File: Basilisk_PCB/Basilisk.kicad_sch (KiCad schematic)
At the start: 58 parts, among them J1 Conn_01x04, J2 HUB75E, J3 Barrel_Jack, J4 USB_C_Receptacle_USB2.0, Q1 S8050, Q2 S8050, SW1 IO0, SW2 RST, U1 AT25SF081-SSHD-X, U2 ESP32-WROOM-32D, U3 MLX90640, U4 TXS0108EPW, U5 TXS0108EPW, U6 TPS54560BDDA, U7 AMS1117-3.3, U8 FT231XS

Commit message: read thermal camera
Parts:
- added R?: PDV-P8103, OptoDevice:R_LDR_5.0x4.1mm_P3mm_Vertical, symbol Sensor_Optical:A9050
- added R?: 53.6k, Resistor_SMD:R_0805_2012Metric, symbol Device:R
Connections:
- net +3.3V: now also R?.1
- net GND: now also R?.1
- net at U2.6 (IO34): now also R?.2, R?.2
- no-connect marks 24 -> 23
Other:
- note added: "500 - 20kOhm"
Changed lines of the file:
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@@
   (junction (at 88.9 189.23) (diameter 0) (color 0 0 0 0)
+  )
+  (junction (at 240.03 90.17) (diameter 0) (color 0 0 0 0)
   )
   (junction (at 242.57 113.03) (diameter 0) (color 0 0 0 0)
@@
   (no_connect (at 77.47 113.03))
   (no_connect (at 227.33 92.71))
-  (no_connect (at 227.33 90.17))
   (no_connect (at 50.8 173.99))
   (no_connect (at 50.8 171.45))
@@
     (stroke (width 0) (type default) (color 0 0 0 0))
   )
+  (wire (pts (xy 227.33 90.17) (xy 240.03 90.17))
+    (stroke (width 0) (type default) (color 0 0 0 0))
+  )
   (wire (pts (xy 240.03 69.85) (xy 240.03 72.39))
     (stroke (width 0) (type default) (color 0 0 0 0))
@@
     (effects (font (size 1.27 1.27)) (justify left bottom))
   )
+  (text "500 - 20kOhm" (at 246.38 85.09 0)
+    (effects (font (size 1.27 1.27)) (justify left bottom))
+  )
   (text "IO7\nIO8\nIO9\nIO10\nIO6\nIO11" (at 210.82 77.47 0)
     (effects (font (size 1.27 1.27)) (justify left bottom))
@@
   (label "E.5" (at 72.39 100.33 0)
     (effects (font (size 1.27 1.27)) (justify left bottom))
+  )
+  (symbol (lib_id "Sensor_Optical:A9050") (at 240.03 86.36 0) (unit 1)
+    (in_bom yes) (on_board yes) (fields_autoplaced)
+    (property "Reference" "R?" (id 0) (at 242.57 85.0899 0)
+      (effects (font (size 1.27 1.27)) (justify left))
+    )
+    (property "Value" "PDV-P8103" (id 1) (at 242.57 87.6299 0)
+      (effects (font (size 1.27 1.27)) (justify left))
+    )
+    (property "Footprint" "OptoDevice:R_LDR_5.0x4.1mm_P3mm_Vertical" (id 2) (at 244.475 86.36 90)
+      (effects (font (size 1.27 1.27)) hide)
+    )
+    (property "Datasheet" "http://cdn-reichelt.de/documents/datenblatt/A500/A90xxxx%23PE.pdf" (id 3) (at 240.03 87.63 0)
+      (effects (font (size 1.27 1.27)) hide)
+    )
+    (pin "1")
+    (pin "2")
   )
   (symbol (lib_id "Device:LED_Small") (at 109.22 176.53 0) (unit 1)
@@
     (pin "2")
   )
+  (symbol (lib_id "Device:R") (at 240.03 93.98 0) (mirror x) (unit 1)
+    (in_bom yes) (on_board yes)
+    (property "Reference" "R?" (id 0) (at 242.57 93.98 90))
+    (property "Value" "53.6k" (id 1) (at 240.03 93.98 90))
+    (property "Footprint" "Resistor_SMD:R_0805_2012Metric" (id 2) (at 238.252 93.98 90)
+      (effects (font (size 1.27 1.27)) hide)
+    )
+    (property "Datasheet" "~" (id 3) (at 240.03 93.98 0)
+      (effects (font (size 1.27 1.27)) hide)
+    )
+    (pin "1")
+    (pin "2")
+  )
   (symbol (lib_id "power:+3.3V") (at 45.72 86.36 0) (unit 1)
     (in_bom yes) (on_board yes)
@@
     )
     (property "Datasheet" "" (id 3) (at 45.72 86.36 0)
+      (effects (font (size 1.27 1.27)) hide)
+    )
+    (pin "1")
+  )
+  (symbol (lib_id "power:+3.3V") (at 240.03 82.55 0) (unit 1)
+    (in_bom yes) (on_board yes)
+    (property "Reference" "#PWR?" (id 0) (at 240.03 86.36 0)
+      (effects (font (size 1.27 1.27)) hide)
+    )
+    (property "Value" "+3.3V" (id 1) (at 240.03 78.74 0))
+    (property "Footprint" "" (id 2) (at 240.03 82.55 0)
+      (effects (font (size 1.27 1.27)) hide)
+    )
+    (property "Datasheet" "" (id 3) (at 240.03 82.55 0)
       (effects (font (size 1.27 1.27)) hide)
     )
@@
     (pin "1")
     (pin "2")
+  )
+  (symbol (lib_id "power:GND") (at 240.03 97.79 0) (unit 1)
+    (in_bom yes) (on_board yes) (fields_autoplaced)
+    (property "Reference" "#PWR?" (id 0) (at 240.03 104.14 0)
+      (effects (font (size 1.27 1.27)) hide)
+    )
+    (property "Value" "GND" (id 1) (at 240.03 102.87 0))
+    (property "Footprint" "" (id 2) (at 240.03 97.79 0)
+      (effects (font (size 1.27 1.27)) hide)
+    )
+    (property "Datasheet" "" (id 3) (at 240.03 97.79 0)
+      (effects (font (size 1.27 1.27)) hide)
+    )
+    (pin "1")
   )
   (symbol (lib_id "power:GND") (at 212.09 100.33 0) (unit 1)
@@
       (reference "#PWR0138") (unit 1) (value "GND") (footprint "")
     )
+    (path "/1a900e92-a8b4-4094-b0db-bd95bb794e53"
+      (reference "#PWR?") (unit 1) (value "+3.3V") (footprint "")
+    )
+    (path "/4d88429a-b5c5-4cab-b654-3b242198df17"
+      (reference "#PWR?") (unit 1) (value "GND") (footprint "")
+    )
     (path "/7bc39325-dda5-44b6-990c-c832c8ee2028"
       (reference "C1") (unit 1) (value "0.1uf") (footprint "Capacitor_SMD:C_0805_2012Metric")
@@
       (reference "R20") (unit 1) (value "270") (footprint "Resistor_SMD:R_0805_2012Metric")
     )
+    (path "/05dc7fc5-dc6e-4fac-841c-11189469d341"
+      (reference "R?") (unit 1) (value "PDV-P8103") (footprint "OptoDevice:R_LDR_5.0x4.1mm_P3mm_Vertical")
+    )
+    (path "/138762a6-fb1c-40a2-9338-c92b2a79b7d5"
+      (reference "R?") (unit 1) (value "53.6k") (footprint "Resistor_SMD:R_0805_2012Metric")
+    )
     (path "/e4667d70-2ef7-4de3-b4b9-08b3601d086e"

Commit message: add CAD model of matrix
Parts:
- gave numbers to parts that had none: 2
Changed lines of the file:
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@@
   (symbol (lib_id "Sensor_Optical:A9050") (at 240.03 86.36 0) (unit 1)
     (in_bom yes) (on_board yes) (fields_autoplaced)
-    (property "Reference" "R?" (id 0) (at 242.57 85.0899 0)
+    (property "Reference" "R21" (id 0) (at 242.57 85.0899 0)
       (effects (font (size 1.27 1.27)) (justify left))
     )
@@
   (symbol (lib_id "Device:R") (at 240.03 93.98 0) (mirror x) (unit 1)
     (in_bom yes) (on_board yes)
-    (property "Reference" "R?" (id 0) (at 242.57 93.98 90))
+    (property "Reference" "R22" (id 0) (at 242.57 93.98 90))
     (property "Value" "53.6k" (id 1) (at 240.03 93.98 90))
     (property "Footprint" "Resistor_SMD:R_0805_2012Metric" (id 2) (at 238.252 93.98 90)
@@
   (symbol (lib_id "power:+3.3V") (at 240.03 82.55 0) (unit 1)
     (in_bom yes) (on_board yes)
-    (property "Reference" "#PWR?" (id 0) (at 240.03 86.36 0)
+    (property "Reference" "#PWR0140" (id 0) (at 240.03 86.36 0)
       (effects (font (size 1.27 1.27)) hide)
     )
@@
   (symbol (lib_id "power:GND") (at 240.03 97.79 0) (unit 1)
     (in_bom yes) (on_board yes) (fields_autoplaced)
-    (property "Reference" "#PWR?" (id 0) (at 240.03 104.14 0)
+    (property "Reference" "#PWR0139" (id 0) (at 240.03 104.14 0)
       (effects (font (size 1.27 1.27)) hide)
     )
@@
       (reference "#PWR0138") (unit 1) (value "GND") (footprint "")
     )
+    (path "/4d88429a-b5c5-4cab-b654-3b242198df17"
+      (reference "#PWR0139") (unit 1) (value "GND") (footprint "")
+    )
     (path "/1a900e92-a8b4-4094-b0db-bd95bb794e53"
-      (reference "#PWR?") (unit 1) (value "+3.3V") (footprint "")
-    )
-    (path "/4d88429a-b5c5-4cab-b654-3b242198df17"
-      (reference "#PWR?") (unit 1) (value "GND") (footprint "")
+      (reference "#PWR0140") (unit 1) (value "+3.3V") (footprint "")
     )
     (path "/7bc39325-dda5-44b6-990c-c832c8ee2028"
@@
     )
     (path "/05dc7fc5-dc6e-4fac-841c-11189469d341"
-      (reference "R?") (unit 1) (value "PDV-P8103") (footprint "OptoDevice:R_LDR_5.0x4.1mm_P3mm_Vertical")
+      (reference "R21") (unit 1) (value "PDV-P8103") (footprint "OptoDevice:R_LDR_5.0x4.1mm_P3mm_Vertical")
     )
     (path "/138762a6-fb1c-40a2-9338-c92b2a79b7d5"
-      (reference "R?") (unit 1) (value "53.6k") (footprint "Resistor_SMD:R_0805_2012Metric")
+      (reference "R22") (unit 1) (value "53.6k") (footprint "Resistor_SMD:R_0805_2012Metric")
     )
     (path "/e4667d70-2ef7-4de3-b4b9-08b3601d086e"

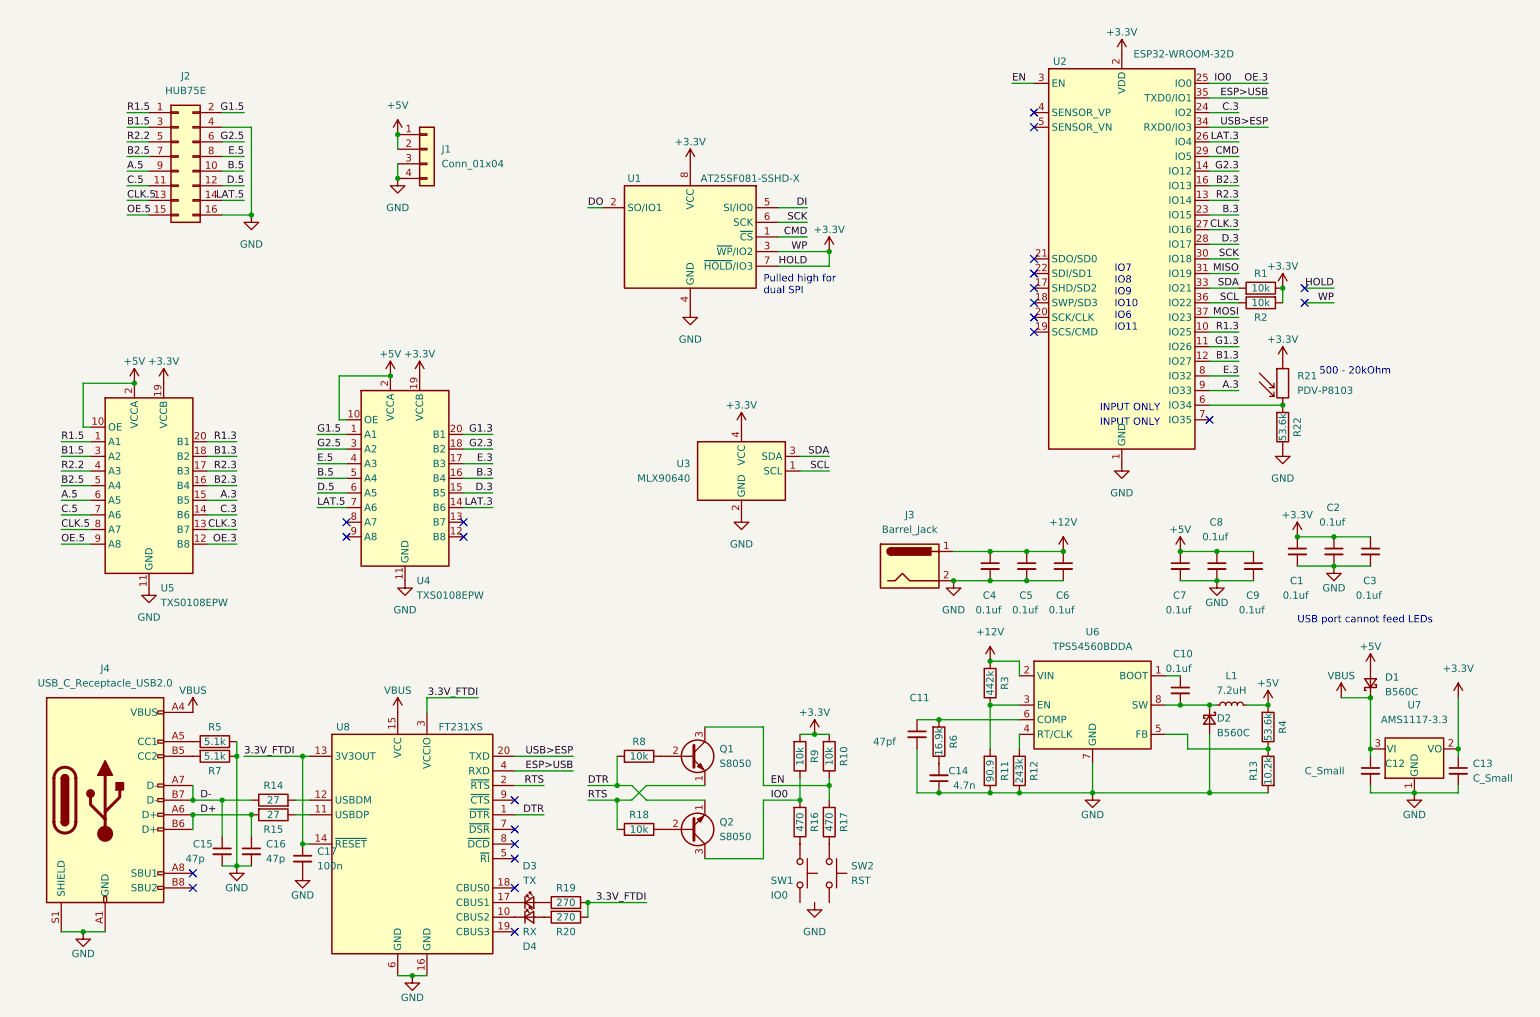
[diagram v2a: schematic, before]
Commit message: set up fixed components on board
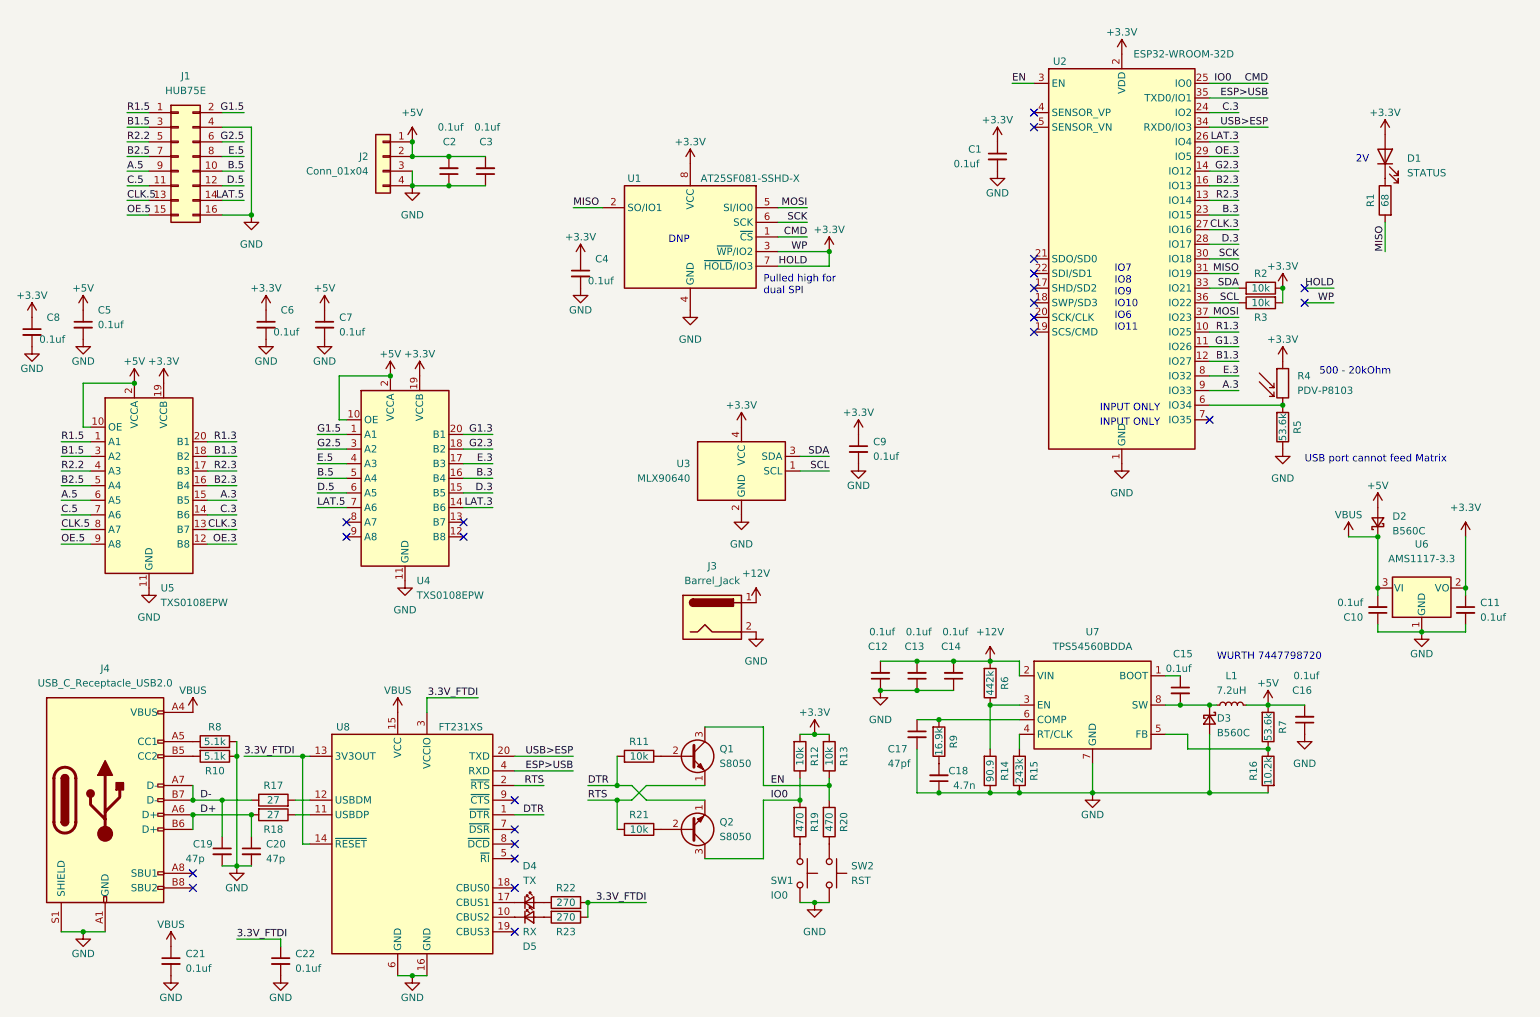
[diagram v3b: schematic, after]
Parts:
- removed C12, C13: C_Small, Capacitor_SMD:C_0805_2012Metric, symbol Device:C_Small
- removed C17: 100n, Capacitor_SMD:C_0805_2012Metric, symbol Device:C_Small
- removed C9: 0.1uf, Capacitor_SMD:C_0805_2012Metric, symbol Device:C_Small
- added C10, C11, C16, C2, C21, C22, C3, C6, C8: 0.1uf, Capacitor_SMD:C_0805_2012Metric, symbol Device:C_Small
- added D1: STATUS, LED_THT:LED_D5.0mm_Clear, symbol Device:LED
- added R1: 68, Resistor_SMD:R_0805_2012Metric, symbol Device:R
- L1: footprint (none) -> Inductor_SMD:L_Wuerth_WE-PDF
- Q1, Q2: footprint Package_TO_SOT_THT:TO-92_Inline -> Package_TO_SOT_SMD:SOT-23
- SW1, SW2: footprint Button_Switch_SMD:SW_SPST_TL3342 -> Button_Switch_SMD:SW_SPST_EVQP7A
- renumbered C6 to C12, C5 to C13, C4 to C14, C10 to C15, C11 to C17, C14 to C18, C15 to C19, C16 to C20, C2 to C4, C7 to C5, C8 to C7, C3 to C9, D1 to D2, D2 to D3, D3 to D4, D4 to D5, J2 to J1, J1 to J2, R7 to R10, R8 to R11, R9 to R12, R10 to R13, R11 to R14, R12 to R15, R13 to R16, R14 to R17, R15 to R18, R16 to R19, R1 to R2, R17 to R20, R18 to R21, R19 to R22, R20 to R23, R2 to R3, R21 to R4, R22 to R5, R3 to R6, R4 to R7, R5 to R8, R6 to R9, U7 to U6, U6 to U7
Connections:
- net DI is gone; now on net MOSI: U1.5 (SI/IO0)
- net DO is gone; now on net MISO: U1.2 (SO/IO1)
- net +12V: now also C12.2, C13.2, C14.2; no longer C12.1, C13.1, C14.1
- net +3.3V: now also C11.1, C6.1, C8.1, D1.2 (A)
- net +5V: now also C16.2, C2.2, C3.2
- net 3.3V_FTDI: now also C22.1
- net CMD: now also Q2.3 (C), R12.1, R19.2, U2.25 (IO0); no longer U2.29 (IO5)
- net GND: now also C12.1, C13.1, C14.1, SW1.2, SW2.2, C10.1, C11.2, C16.1, C2.1, C21.2, C22.2, C3.1, C6.2, C8.2; no longer C12.2, C13.2, C14.2
- net MISO: now also R1.2
- net VBUS: now also C10.2, C21.1
- removed net IO0: Q2.3 (C), R12.1, R19.2, U2.25 (IO0), U5.12 (B8)
- new net: D1.1 (K), R1.1
- new net OE.3: U2.29 (IO5), U5.12 (B8)
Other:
- note added: "2V"
- note added: "DNP"
- note added: "USB port cannot feed Matrix"
- note added: "WURTH 7447798720"
- note removed: "USB port cannot feed LEDs"
- moved on the sheet: C1, C12, C13, C14, C4, C5, C7, C9, D2, J2, J3, U6

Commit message: Routed PCB
Routed most of PCB
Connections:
- net A.3: now also U5.14 (B6); no longer U5.15 (B5)
- net A.5: now also U5.7 (A6); no longer U5.6 (A5)
- net B.3: now also U2.29 (IO5), U5.13 (B7); no longer U2.23 (IO15), U4.16 (B4)
- net B.5: now also U5.8 (A7); no longer U4.5 (A4)
- net B1.3: now also U4.14 (B6); no longer U5.18 (B2)
- net B1.5: now also U4.7 (A6); no longer U5.3 (A2)
- net B2.3: now also U4.17 (B3); no longer U5.16 (B4)
- net B2.5: now also U4.4 (A3); no longer U5.5 (A4)
- net C.3: now also U5.16 (B4); no longer U5.14 (B6)
- net C.5: now also U5.5 (A4); no longer U5.7 (A6)
- net CLK.3: now also U5.18 (B2); no longer U5.13 (B7)
- net CLK.5: now also U5.3 (A2); no longer U5.8 (A7)
- net D.3: now also U5.15 (B5); no longer U4.15 (B5)
- net D.5: now also U5.6 (A5); no longer U4.6 (A5)
- net E.3: now also U5.12 (B8); no longer U4.17 (B3)
- net E.5: now also U5.9 (A8); no longer U4.4 (A3)
- net G1.3: now also U4.13 (B7); no longer U4.20 (B1)
- net G1.5: now also U4.8 (A7); no longer U4.1 (A1)
- net G2.3: now also U4.16 (B4); no longer U4.18 (B2)
- net G2.5: now also U4.5 (A4); no longer U4.3 (A2)
- net LAT.3: now also U5.17 (B3); no longer U4.14 (B6)
- net LAT.5: now also U5.4 (A3); no longer U4.7 (A6)
- net OE.3: now also U2.23 (IO15), U5.20 (B1); no longer U2.29 (IO5), U5.12 (B8)
- net OE.5: now also U5.1 (A1); no longer U5.9 (A8)
- net R1.3: now also U4.12 (B8); no longer U5.20 (B1)
- net R1.5: now also U4.9 (A8); no longer U5.1 (A1)
- net R2.3: now also U4.15 (B5); no longer U5.17 (B3)
- net R2.2 renamed R2.5
- net R2.5: now also U4.6 (A5); no longer U5.4 (A3)
- no-connect marks 23 -> 19
